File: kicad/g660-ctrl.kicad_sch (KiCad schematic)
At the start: 0 parts

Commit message: feat: Implement G_CW logic
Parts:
- added D1, D2, D3, D4, D5, D6, D7, D8, D9: 1N4148, Diode_THT:D_DO-35_SOD27_P7.62mm_Horizontal, symbol Diode:1N4148
- added Q1, Q2, Q3, Q4, Q5: NPN, symbol Simulation_SPICE:NPN
- added R1, R2, R3, R4: 100k, symbol Device:R
- added R10, R11, R9: 2.2k, symbol Device:R
- added R5, R6, R7, R8: 22k, symbol Device:R
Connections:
- new net: D3.2 (A), D4.2 (A), R2.2, R7.1
- new net: Q3.2 (B), R7.2
- new net: D5.2 (A), D6.2 (A), R3.2, R8.1
- new net: D7.2 (A), D8.2 (A), D9.2 (A), R4.2, R6.1
- new net: Q2.2 (B), R6.2
- new net: Q1.1 (C), Q2.1 (C), R11.2, R9.1
- new net: Q5.2 (B), R9.2
- new net: D1.2 (A), D2.2 (A), R1.2, R5.1
- new net: Q4.2 (B), R8.2
- new net: Q1.2 (B), R5.2
- new net !SW_N: D1.1 (K), D7.1 (K)
- new net +12V: R1.1, R10.1, R11.1, R2.1, R3.1, R4.1
- new net GND: Q1.3 (E), Q2.3 (E), Q3.3 (E), Q4.3 (E), Q5.3 (E)
- new net G_CW: Q3.1 (C), Q4.1 (C), Q5.1 (C), R10.2
- new net SIG_K: D5.1 (K)
- new net SIG_L: D3.1 (K), D9.1 (K)
- new net SIG_N: D2.1 (K)
- new net SW_K: D6.1 (K), D8.1 (K)
- new net SW_L: D4.1 (K)
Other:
- note added: "COND-A"
- note added: "COND-B"
- note added: "KILL-1"
- note added: "KILL-2"
- company: (none) -> Aiden Cherniske | Bucknell Bison Racing
- title: (none) -> g660-ctrl

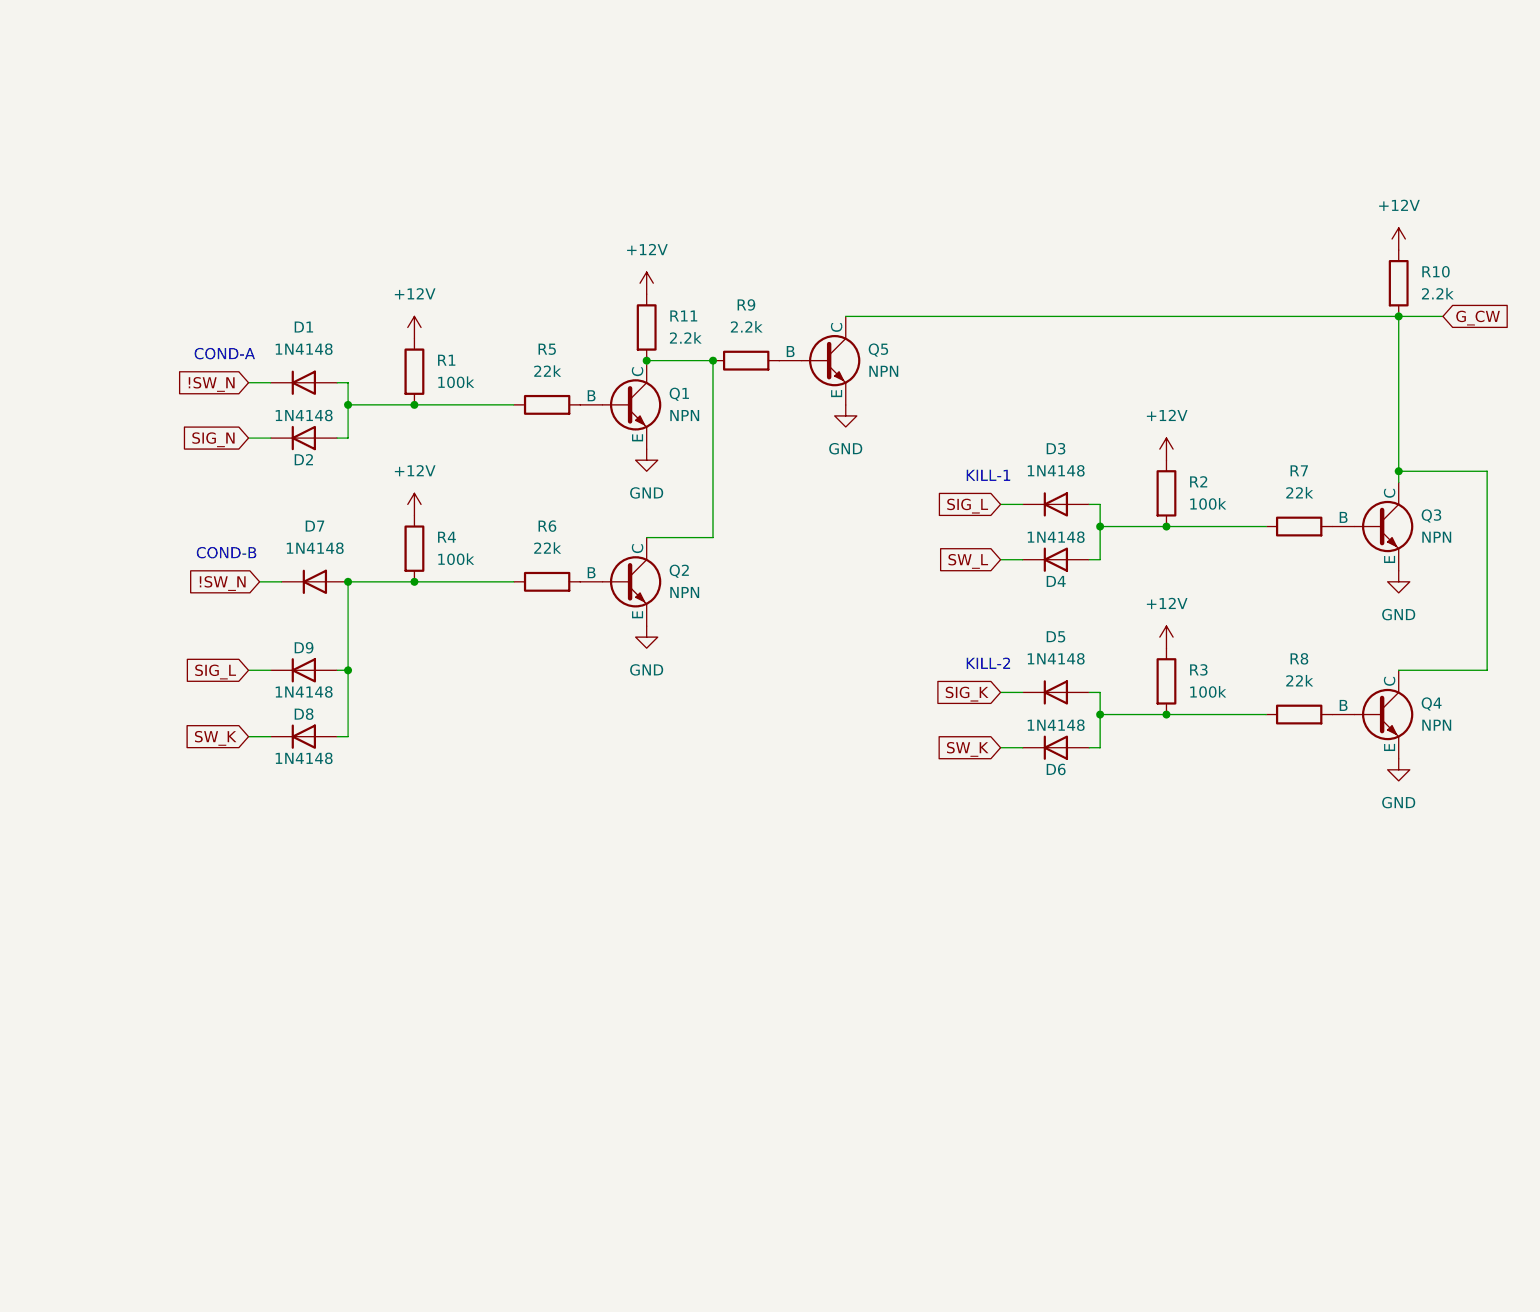
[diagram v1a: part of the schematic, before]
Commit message: style: Clean up schematic and reassign designators
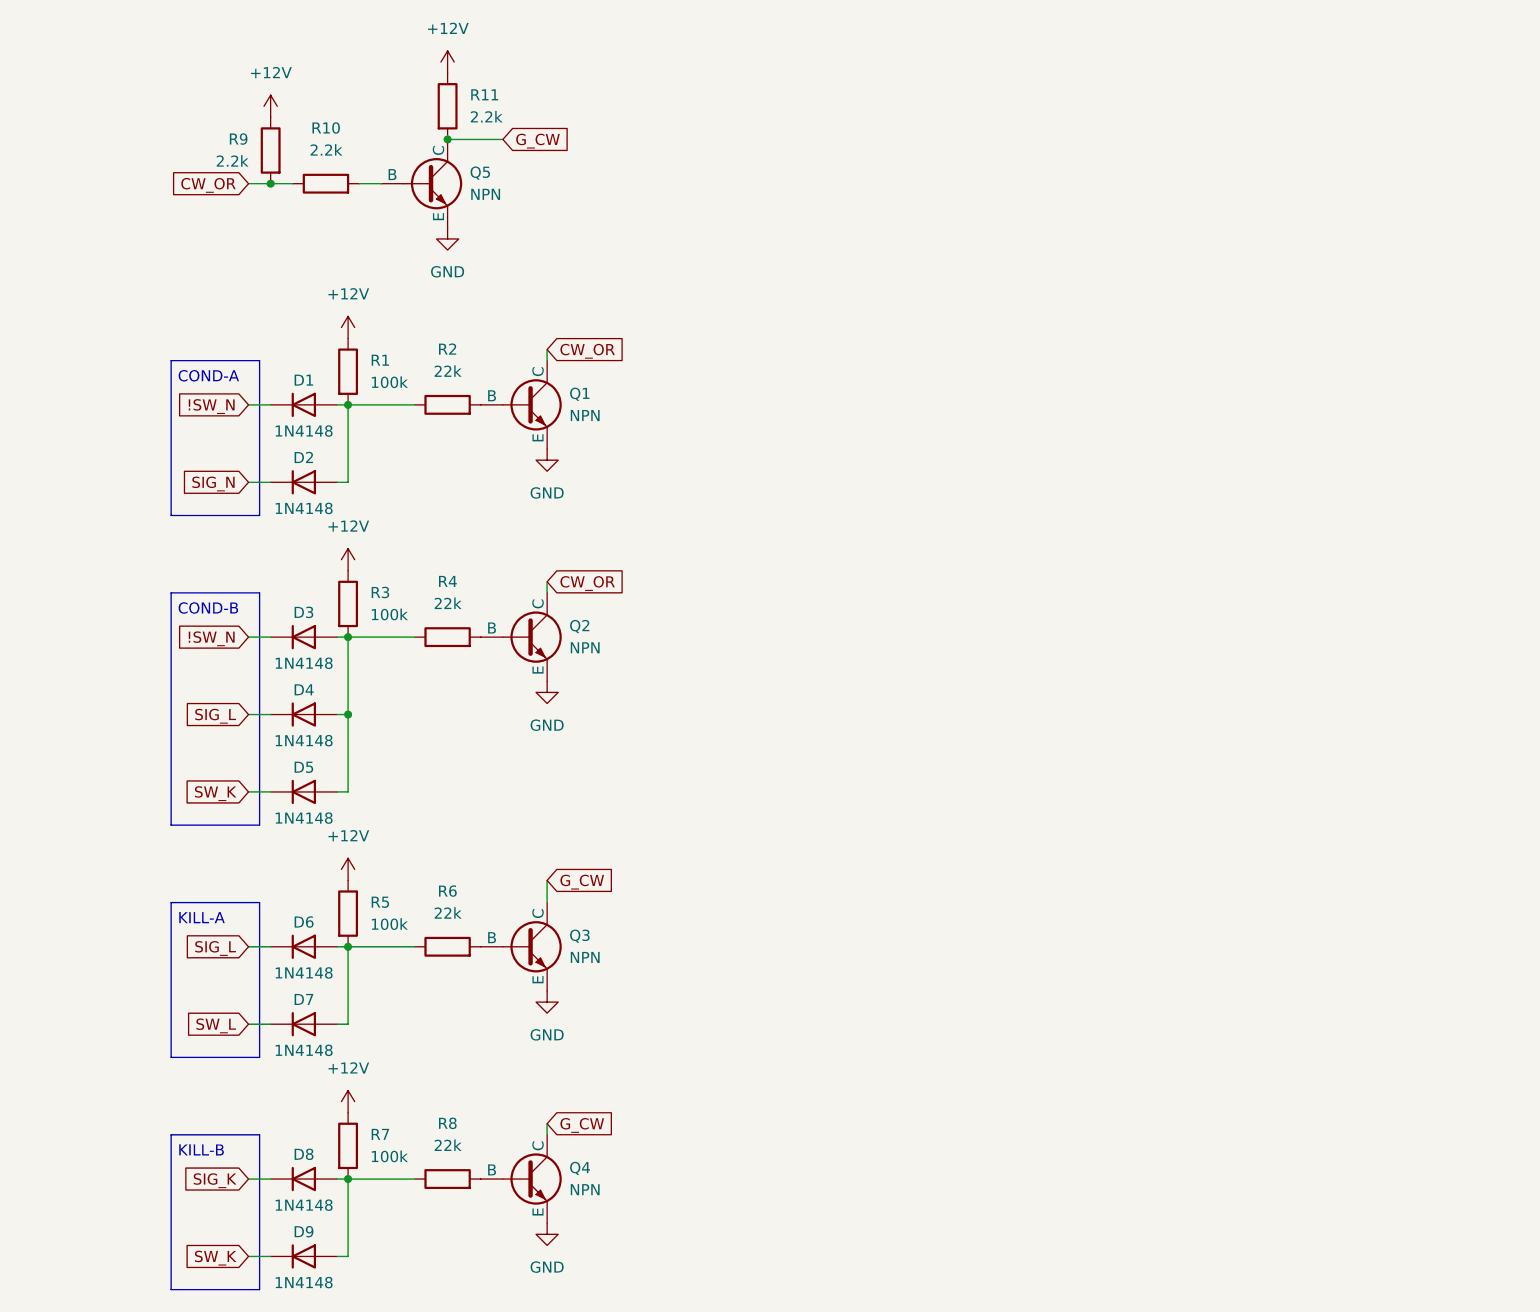
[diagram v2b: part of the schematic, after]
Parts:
- renumbered R9 to R10, R10 to R11, R5 to R2, R4 to R3, R6 to R4, R2 to R5, R7 to R6, R3 to R7, R11 to R9
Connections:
- net !SW_N: now also D3.1 (K); no longer D7.1 (K)
- net SIG_K: now also D8.1 (K); no longer D5.1 (K)
- net SIG_L: now also D4.1 (K), D6.1 (K); no longer D3.1 (K), D9.1 (K)
- net SW_K: now also D5.1 (K), D9.1 (K); no longer D6.1 (K), D8.1 (K)
- net SW_L: now also D7.1 (K); no longer D4.1 (K)
- net at D3.2 (A), D4.2 (A): now also D5.2 (A), R3.2, R4.1; no longer R5.2, R6.1
- net at R7.2, R8.1: now also D8.2 (A), D9.2 (A); no longer D5.2 (A), D6.2 (A)
- net CW_OR: now reaches Q1.1 (C), Q2.1 (C), R10.1, R9.2
- new net: D6.2 (A), D7.2 (A), R5.2, R6.1
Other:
- note added: "KILL-A"
- note added: "KILL-B"
- note removed: "KILL-1"
- note removed: "KILL-2"
- moved on the sheet: D1, Q1, Q2, Q3, Q4, Q5, R1, R10, R11, R2, R3, R4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

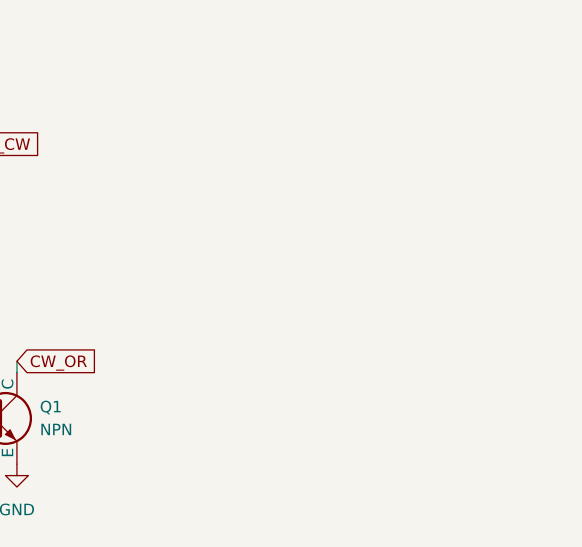
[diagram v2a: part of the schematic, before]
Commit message: feat: Add SW_N inverter circuit
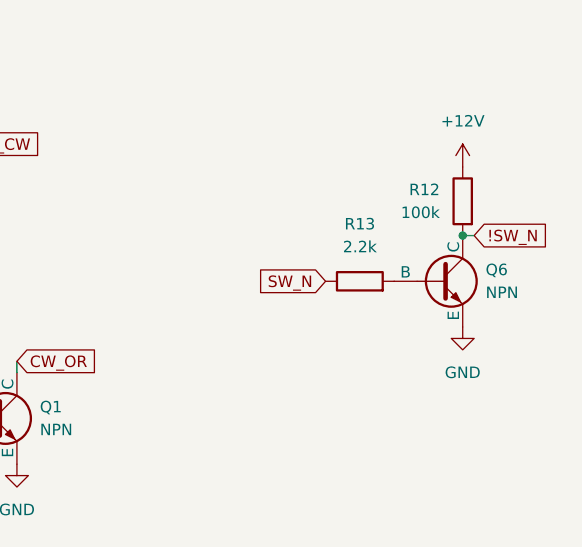
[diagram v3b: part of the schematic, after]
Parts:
- added Q6: NPN, symbol Simulation_SPICE:NPN
- added R12: 100k, symbol Device:R
- added R13: 2.2k, symbol Device:R
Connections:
- net !SW_N: now also Q6.1 (C), R12.2
- net +12V: now also R12.1
- net GND: now also Q6.3 (E)
- net SW_N: now also R13.1
- new net: Q6.2 (B), R13.2

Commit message: feat: Implement CCW logic
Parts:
- added D10, D11, D12, D13, D14, D15, D16, D17, D18, D19, D20: 1N4148, Diode_THT:D_DO-35_SOD27_P7.62mm_Horizontal, symbol Diode:1N4148
- added Q10, Q11, Q12, Q7, Q8, Q9: NPN, symbol Simulation_SPICE:NPN
- added R14, R16, R18, R20, R22: 100k, symbol Device:R
- added R15, R17, R19, R21, R23, R26: 22k, symbol Device:R
- added R24, R25: 2.2k, symbol Device:R
- R10, R13: value 2.2k -> 22k
- R12: value 100k -> 2.2k
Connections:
- net !SW_N: now also D20.1 (K)
- net +12V: now also R14.1, R16.1, R18.1, R20.1, R22.1, R24.1, R25.1
- net GND: now also Q10.3 (E), Q11.3 (E), Q12.3 (E), Q7.3 (E), Q8.3 (E), Q9.3 (E)
- net SIG_K: now also D11.1 (K), D13.1 (K)
- net SIG_L: now also D15.1 (K), D19.1 (K)
- net SIG_N: now also D17.1 (K)
- net SW_L: now also D12.1 (K), D18.1 (K)
- net SW_N: now also D10.1 (K), D14.1 (K), D16.1 (K)
- new net: D14.2 (A), D15.2 (A), R18.2, R19.1
- new net: Q9.2 (B), R19.2
- new net: D10.2 (A), D11.2 (A), R14.2, R15.1
- new net: Q7.2 (B), R15.2
- new net: D16.2 (A), D17.2 (A), R20.2, R21.1
- new net: D18.2 (A), D19.2 (A), D20.2 (A), R22.2, R23.1
- new net: Q10.2 (B), R21.2
- new net: D12.2 (A), D13.2 (A), R16.2, R17.1
- new net: Q8.2 (B), R17.2
- new net: Q11.2 (B), R23.2
- new net: Q12.2 (B), R26.2
- new net CCW_OR: Q7.1 (C), Q8.1 (C), Q9.1 (C), R25.2, R26.1
- new net G_CCW: Q10.1 (C), Q11.1 (C), Q12.1 (C), R24.2
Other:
- note added: "COND-C"
